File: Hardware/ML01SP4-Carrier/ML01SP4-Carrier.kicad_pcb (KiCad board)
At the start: 2 copper layers, 21 x 20.2 mm, 3 parts, among them J1 NRF24L01P-ML01SP4, J2 Conn_01x05, J3 Conn_01x03

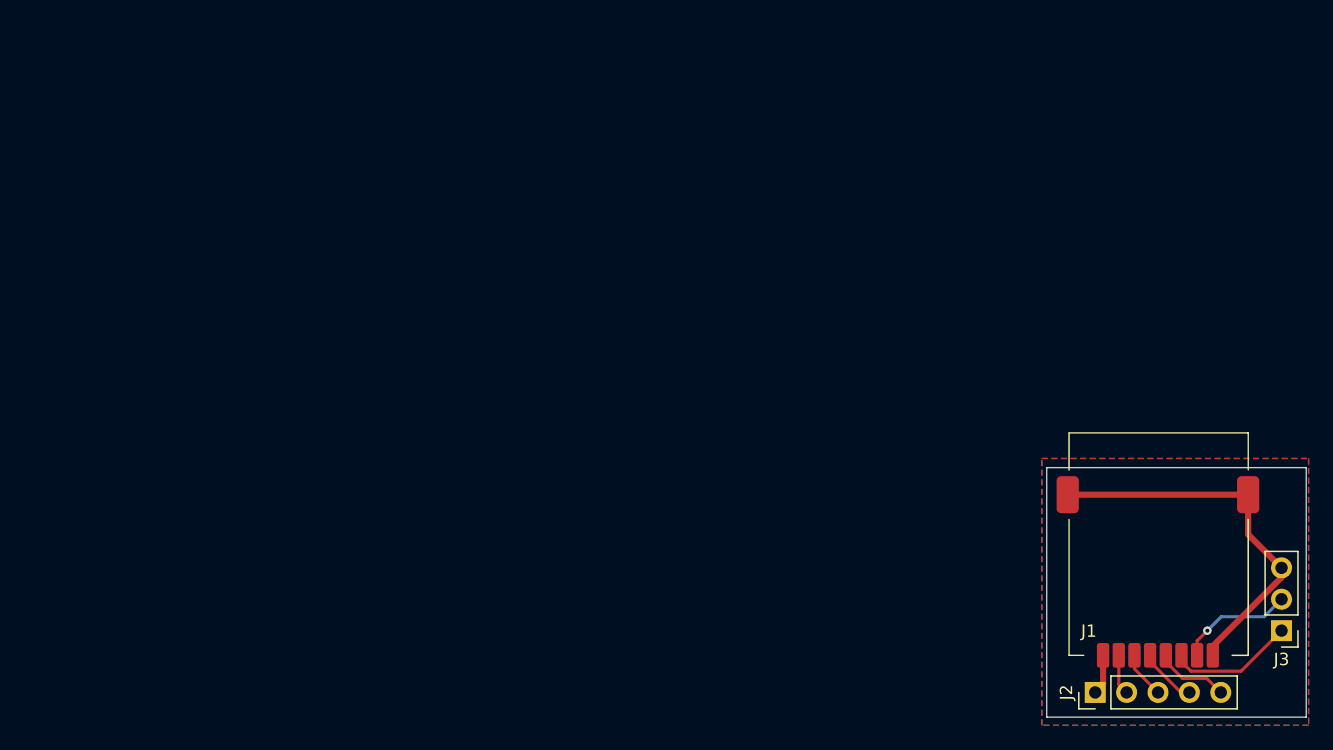
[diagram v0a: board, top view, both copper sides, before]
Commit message: added decoupling capacitors and rounded pcb corners
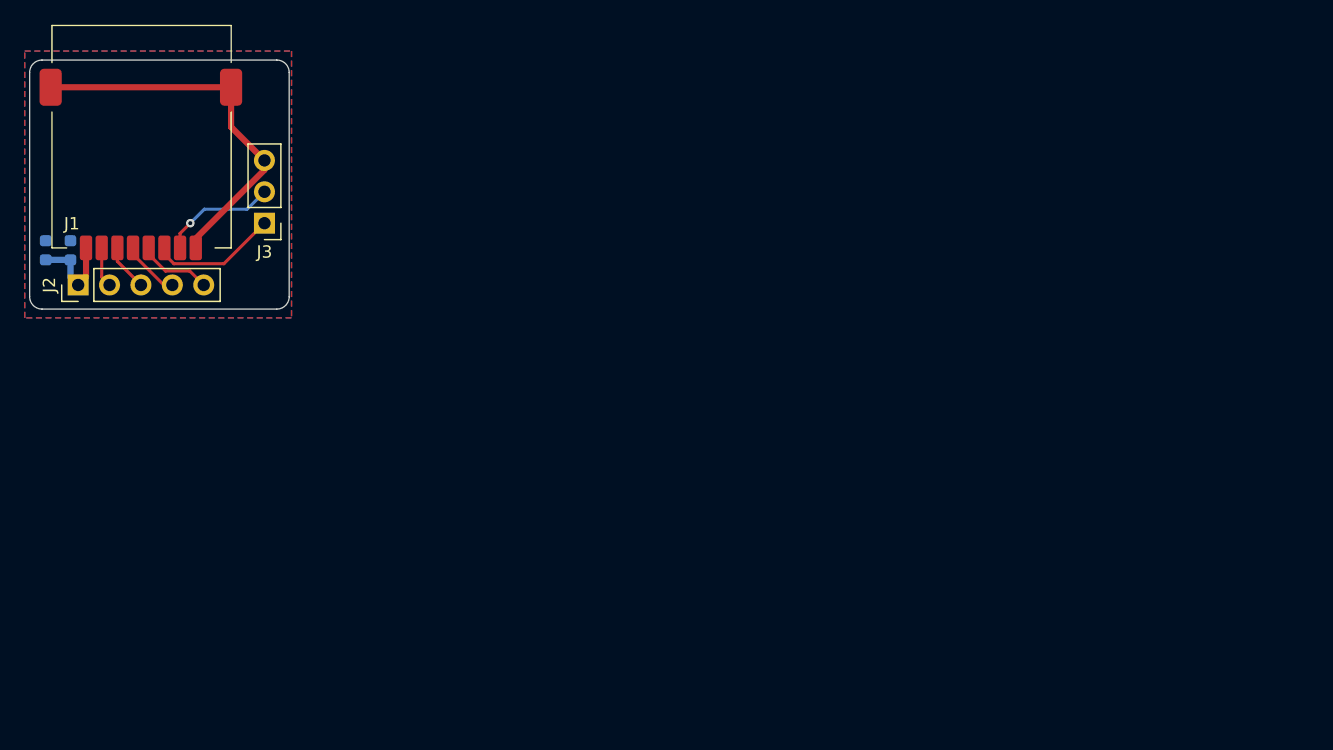
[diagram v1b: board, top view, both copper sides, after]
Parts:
- added C1: 0.1uF, Capacitor_SMD:C_0603_1608Metric, B.Cu at (21.0, 35.2)
- added C2: 4.7uF, Capacitor_SMD:C_0603_1608Metric, B.Cu at (23.0, 35.2)
- moved J1 88.7 mm to (28.7, 35.0)
- moved J2 88.7 mm to (23.6, 38.0)
- moved J3 88.7 mm to (38.7, 33.0)
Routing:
- net +3V3: track 3.26 -> 7.55 mm
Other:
- board size 21 x 20.2 mm -> 21 x 20.1 mm

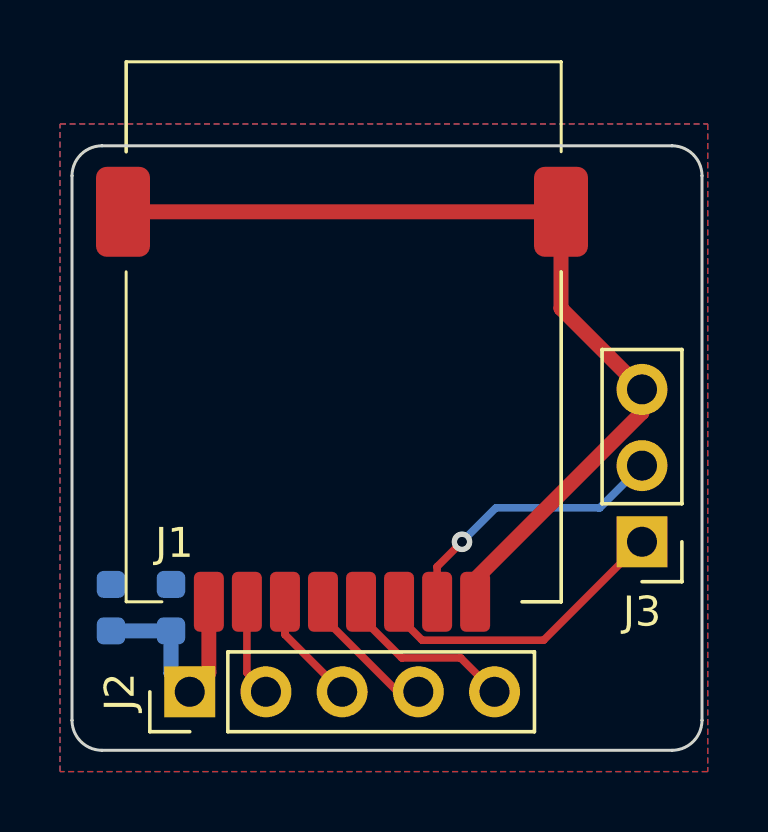
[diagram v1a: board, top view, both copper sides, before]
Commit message: Layout modified, notch on edge cuts layer added.
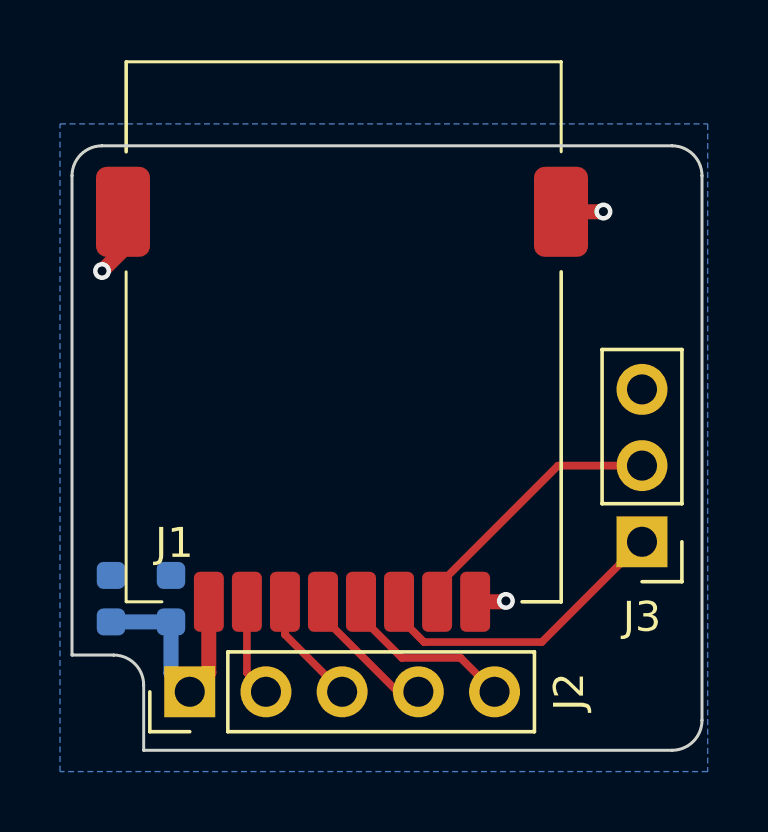
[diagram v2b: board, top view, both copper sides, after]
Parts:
- moved C1 0.30 mm to (21.0, 34.9)
- moved C2 0.30 mm to (23.0, 34.9)
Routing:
- net GND: track 31.0 -> 4.72 mm, vias 0 -> 3
- net Net-(J1-Pad7): track 9.40 -> 9.01 mm, vias 1 -> 0
- removed copper zone on F.Cu, net GND
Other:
- outline, holes or cut-outs redrawn
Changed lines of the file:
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@@
     (property "Sheetname" "")
     (attr through_hole)
-    (fp_text reference "J3" (at 0 -2.33) (layer "F.SilkS")
+    (fp_text reference "J3" (at 0 -2.5046) (layer "F.SilkS")
       (effects (font (size 1 1) (thickness 0.15)))
     )
@@
     (property "Sheetname" "")
     (attr through_hole)
-    (fp_text reference "J2" (at 0 -2.33 90) (layer "F.SilkS")
+    (fp_text reference "J2" (at 0.0062 12.6462 90) (layer "F.SilkS")
       (effects (font (size 1 1) (thickness 0.15)))
     )
@@
   )
   (footprint "Capacitor_SMD:C_0603_1608Metric" (layer "B.Cu")
-    (at 23 35.225 90)
+    (at 23 34.925 90)
     (descr "Capacitor SMD 0603 (1608 Metric), square (rectangular) end terminal, IPC_7351 nominal, (Body size source: IPC-SM-782 page 76, https://www.pcb-3d.com/wordpress/wp-content/uploads/ipc-sm-782a_amendment_1_and_2.pdf), generated with kicad-footprint-generator")
     (tags "capacitor")
@@
     (property "Sheetname" "")
     (attr smd)
-    (fp_text reference "C2" (at 0 1.43 90) (layer "B.SilkS")
+    (fp_text reference "C2" (at 2.413 0.0124 90) (layer "B.SilkS")
       (effects (font (size 1 1) (thickness 0.15)) (justify mirror))
     )
@@
   )
   (footprint "Capacitor_SMD:C_0603_1608Metric" (layer "B.Cu")
-    (at 21 35.225 90)
+    (at 21 34.925 90)
     (descr "Capacitor SMD 0603 (1608 Metric), square (rectangular) end terminal, IPC_7351 nominal, (Body size source: IPC-SM-782 page 76, https://www.pcb-3d.com/wordpress/wp-content/uploads/ipc-sm-782a_amendment_1_and_2.pdf), generated with kicad-footprint-generator")
     (tags "capacitor")
@@
     (property "Sheetname" "")
     (attr smd)
-    (fp_text reference "C1" (at 0 1.43 90) (layer "B.SilkS")
+    (fp_text reference "C1" (at 2.413 -0.0196 90) (layer "B.SilkS")
       (effects (font (size 1 1) (thickness 0.15)) (justify mirror))
     )
@@
     )
   )
-  (gr_arc (start 20.7 39.98) (mid 19.992893 39.687107) (end 19.7 38.98) (layer "Edge.Cuts") (width 0.1))
+  (gr_line (start 21.088893 36.805107) (end 19.7 36.805107) (layer "Edge.Cuts") (width 0.1))
+  (gr_arc (start 40.7 38.98) (mid 40.407107 39.687107) (end 39.7 39.98) (layer "Edge.Cuts") (width 0.1))
+  (gr_line (start 22.088893 39.98) (end 39.7 39.98) (layer "Edge.Cuts") (width 0.1))
+  (gr_arc (start 19.7 20.83) (mid 19.992893 20.122893) (end 20.7 19.83) (layer "Edge.Cuts") (width 0.1))
   (gr_line (start 40.7 20.83) (end 40.7 38.98) (layer "Edge.Cuts") (width 0.1))
+  (gr_line (start 22.088893 37.805107) (end 22.088893 39.98) (layer "Edge.Cuts") (width 0.1))
+  (gr_arc (start 21.088893 36.805107) (mid 21.796 37.098) (end 22.088893 37.805107) (layer "Edge.Cuts") (width 0.1))
+  (gr_line (start 19.7 20.83) (end 19.7 36.805107) (layer "Edge.Cuts") (width 0.1))
+  (gr_arc (start 39.7 19.83) (mid 40.407107 20.122893) (end 40.7 20.83) (layer "Edge.Cuts") (width 0.1))
   (gr_line (start 20.7 19.83) (end 39.7 19.83) (layer "Edge.Cuts") (width 0.1))
-  (gr_line (start 19.7 38.98) (end 19.7 20.83) (layer "Edge.Cuts") (width 0.1))
-  (gr_line (start 39.7 39.98) (end 20.7 39.98) (layer "Edge.Cuts") (width 0.1))
-  (gr_arc (start 39.7 19.83) (mid 40.407107 20.122893) (end 40.7 20.83) (layer "Edge.Cuts") (width 0.1))
-  (gr_arc (start 40.7 38.98) (mid 40.407107 39.687107) (end 39.7 39.98) (layer "Edge.Cuts") (width 0.1))
-  (gr_arc (start 19.7 20.83) (mid 19.992893 20.122893) (end 20.7 19.83) (layer "Edge.Cuts") (width 0.1))
   (segment (start 24.262 35.03) (end 24.262 37.393) (width 0.5) (layer "F.Cu") (net 1))
   (segment (start 24.262 37.393) (end 23.625 38.03) (width 0.5) (layer "F.Cu") (net 1))
+  (segment (start 23 35.7) (end 23 37.405) (width 0.5) (layer "B.Cu") (net 1))
+  (segment (start 21 35.7) (end 23 35.7) (width 0.5) (layer "B.Cu") (net 1))
   (segment (start 23 37.405) (end 23.625 38.03) (width 0.5) (layer "B.Cu") (net 1))
-  (segment (start 23 36) (end 23 37.405) (width 0.5) (layer "B.Cu") (net 1))
-  (segment (start 21 36) (end 23 36) (width 0.5) (layer "B.Cu") (net 1))
   (segment (start 25.53 37.395) (end 26.165 38.03) (width 0.254) (layer "F.Cu") (net 2))
   (segment (start 25.53 35.03) (end 25.53 37.395) (width 0.254) (layer "F.Cu") (net 2))
@@
   (segment (start 32.6556 36.9006) (end 33.785 38.03) (width 0.254) (layer "F.Cu") (net 5))
   (segment (start 30.694626 36.9006) (end 32.6556 36.9006) (width 0.254) (layer "F.Cu") (net 5))
-  (segment (start 38.7 28.718838) (end 38.7 27.95) (width 0.5) (layer "F.Cu") (net 6))
-  (segment (start 36 22.03) (end 21.4 22.03) (width 0.5) (layer "F.Cu") (net 6))
-  (segment (start 38.7 27.95) (end 36 25.25) (width 0.5) (layer "F.Cu") (net 6))
-  (segment (start 36 25.25) (end 36 22.03) (width 0.5) (layer "F.Cu") (net 6))
-  (segment (start 33.138 35.03) (end 33.138 34.280838) (width 0.5) (layer "F.Cu") (net 6))
-  (segment (start 33.138 34.280838) (end 38.7 28.718838) (width 0.5) (layer "F.Cu") (net 6))
-  (segment (start 31.371426 36.3094) (end 35.4206 36.3094) (width 0.254) (layer "F.Cu") (net 7))
-  (segment (start 35.4206 36.3094) (end 38.7 33.03) (width 0.254) (layer "F.Cu") (net 7))
+  (segment (start 36 22.03) (end 37.406 22.03) (width 0.5) (layer "F.Cu") (net 6))
+  (segment (start 21.4 23.304) (end 20.701 24.003) (width 0.5) (layer "F.Cu") (net 6))
+  (segment (start 21.4 22.03) (end 21.4 23.304) (width 0.5) (layer "F.Cu") (net 6))
+  (segment (start 34.1342 35.03) (end 34.163 35.0012) (width 0.5) (layer "F.Cu") (net 6))
+  (segment (start 33.138 35.03) (end 34.1342 35.03) (width 0.5) (layer "F.Cu") (net 6))
+  (segment (start 37.406 22.03) (end 37.4142 22.0218) (width 0.5) (layer "F.Cu") (net 6))
+  (via (at 37.4142 22.0218) (size 0.6) (drill 0.3) (layers "F.Cu" "B.Cu") (net 6))
+  (via (at 34.163 35.0012) (size 0.6) (drill 0.3) (layers "F.Cu" "B.Cu") (net 6))
+  (via (at 20.701 24.003) (size 0.6) (drill 0.3) (layers "F.Cu" "B.Cu") (net 6))
+  (segment (start 30.602 35.539974) (end 31.434826 36.3728) (width 0.254) (layer "F.Cu") (net 7))
   (segment (start 30.602 35.03) (end 30.602 35.539974) (width 0.254) (layer "F.Cu") (net 7))
-  (segment (start 30.602 35.539974) (end 31.371426 36.3094) (width 0.254) (layer "F.Cu") (net 7))
-  (segment (start 31.87 33.86) (end 32.7 33.03) (width 0.254) (layer "F.Cu") (net 8))
-  (segment (start 31.87 35.03) (end 31.87 33.86) (width 0.254) (layer "F.Cu") (net 8))
-  (via (at 32.7 33.03) (size 0.6858) (drill 0.3302) (layers "F.Cu" "B.Cu") (net 8))
-  (segment (start 32.7 33.03) (end 33.8294 31.9006) (width 0.254) (layer "B.Cu") (net 8))
-  (segment (start 33.8294 31.9006) (end 37.2894 31.9006) (width 0.254) (layer "B.Cu") (net 8))
-  (segment (start 37.2894 31.9006) (end 38.7 30.49) (width 0.254) (layer "B.Cu") (net 8))
-  (zone (net 6) (net_name "GND") (layer "F.Cu") (hatch edge 0.508)
-    (connect_pads (clearance 0.508))
-    (min_thickness 0.254) (filled_areas_thickness no)
-    (fill yes (thermal_gap 0.508) (thermal_bridge_width 0.508))
-    (polygon
-      (pts
-        (xy 40.89 40.69)
-        (xy 19.3 40.69)
-        (xy 19.3 19.1)
-        (xy 40.89 19.1)
-      )
-    )
-  )
+  (segment (start 31.434826 36.3728) (end 35.3572 36.3728) (width 0.254) (layer "F.Cu") (net 7))
+  (segment (start 35.3572 36.3728) (end 38.7 33.03) (width 0.254) (layer "F.Cu") (net 7))
+  (segment (start 31.87 35.03) (end 31.87 34.520026) (width 0.254) (layer "F.Cu") (net 8))
+  (segment (start 31.87 34.520026) (end 35.900026 30.49) (width 0.254) (layer "F.Cu") (net 8))
+  (segment (start 35.900026 30.49) (end 38.7 30.49) (width 0.254) (layer "F.Cu") (net 8))
   (zone (net 6) (net_name "GND") (layer "B.Cu") (hatch edge 0.508)
     (connect_pads (clearance 0.508))
@@
     )
   )
-  (group "" (id dbeccf67-64aa-431d-a402-82da2e39ef34)
+  (group "" (id 1400a9fd-21df-4922-a527-197d7282b3da)
     (members
-      026cae32-e5bc-40ce-816d-c33070950ea4
-      19bc858f-a7ae-43a1-9a9f-ac02a1588844
-      2de5bffe-01a6-43f3-b1bf-83e0eb26230a
-      7bb8c804-616d-49aa-a6d8-886058500f8d
-      9fe00901-f64c-46f0-88dc-d9a11d86c389
-      b2577a46-a40c-4218-918f-3e9cb37e78d0
-      c6970708-7895-413a-9e99-29264df189ef
-      ee96299f-ef39-4c25-88a3-2a1594329d82
-    )
-  )
+      0819d038-b721-4946-a6bd-c300d73c2f9a
+      19b90b0d-7c63-4afe-a3eb-7fe68a69ca3b
+      28c20eb7-cc91-49ea-ac5b-1c2d978f1b57
+      43132070-f452-4800-bb3a-08d6ce36bf2d
+      559c6540-319c-419c-b936-e54208c340eb
+      57705bd4-d17a-42ae-b0a1-2f75d3fbf4cc
+      8071ffbc-6a42-41c3-b48d-f75cf2c6af38
+      c10de77b-51a1-4027-a952-cd3bdf69035d
+      c3abbd5e-6101-4bc0-a4a0-48ff095c8a16
+      e4835de9-f5ab-4ae0-acc9-f40b693c59bd
+    )
+  )
